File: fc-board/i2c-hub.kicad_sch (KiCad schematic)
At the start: 54 parts, among them U2 PCT2075TP_147, U3 MAX11617EEE+, U4 DS3231M+TRL, U5 TLV9004QPWRQ1, U6 ADS122C04IPWR

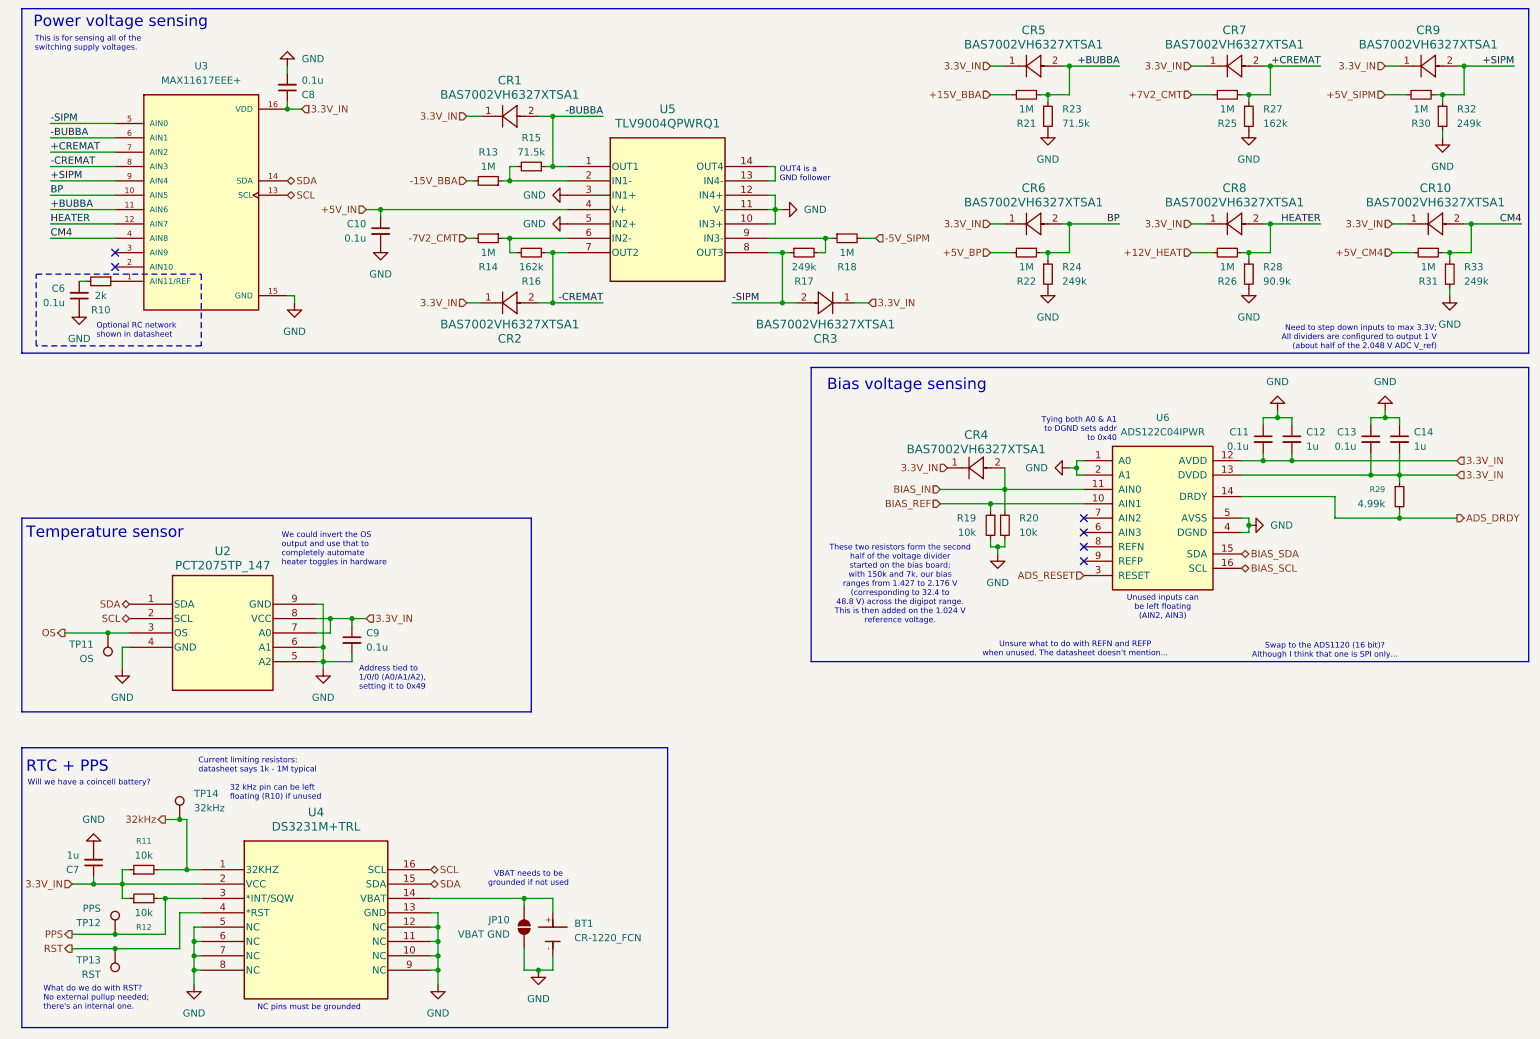
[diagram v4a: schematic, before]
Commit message: Fixed PCIe routing, voltage sensing, added DAQ toggle, LCT interrupt, bias sensing resistors, SD card, and more
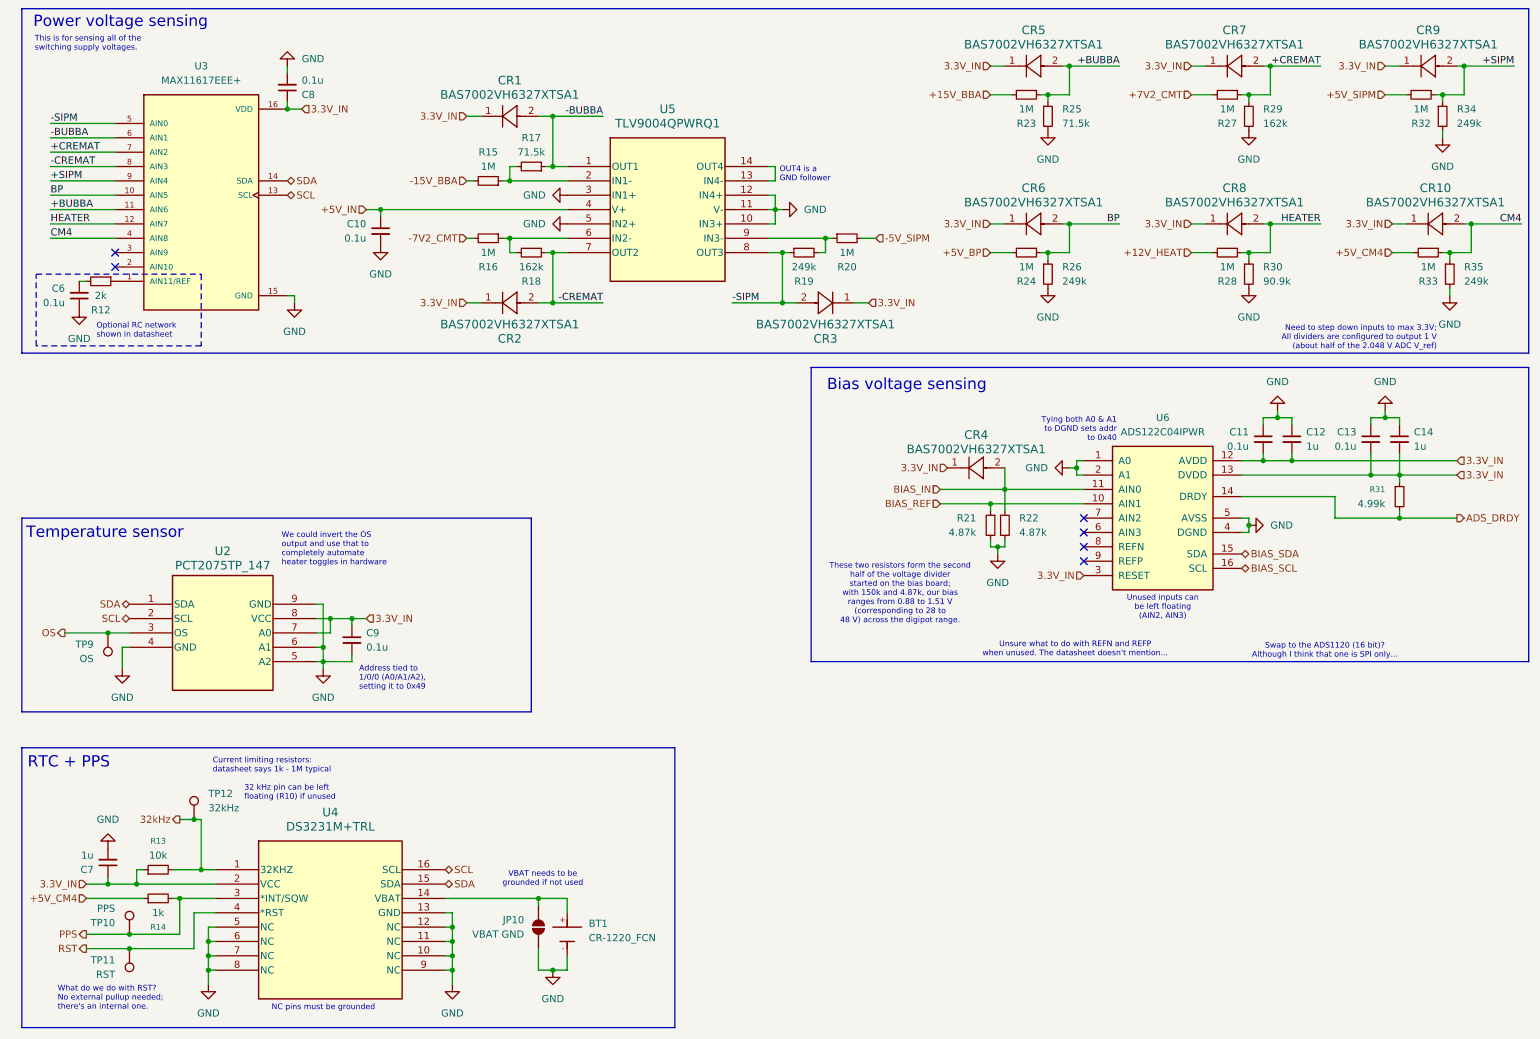
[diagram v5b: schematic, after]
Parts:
- R14: renamed from R12; value 10k -> 1k
- R21: renamed from R19; value 10k -> 4.87k
- R22: renamed from R20; value 10k -> 4.87k
- renumbered R10 to R12, R11 to R13, R13 to R15, R14 to R16, R15 to R17, R16 to R18, R17 to R19, R18 to R20, R21 to R23, R22 to R24, R23 to R25, R24 to R26, R25 to R27, R26 to R28, R27 to R29, R28 to R30, R29 to R31, R30 to R32, R31 to R33, R32 to R34, R33 to R35, TP12 to TP10, TP13 to TP11, TP14 to TP12, TP11 to TP9
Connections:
- net ADS_RESET is gone; now on net 3.3V_IN: U6.3 (RESET)
- net +5V_CM4: now also R14.1
- net 3.3V_IN: no longer R14.1
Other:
- note added: "These two resistors form the second half of the voltage divider started on the bias board; with 150k and 4.87k, our bias ranges from 0.88 to 1.51 V (corresponding to 28 to 48 V) across the digipot range."
- note removed: "These two resistors form the second half of the voltage divider started on the bias board; with 150k and 7k, our bias ranges from 1.427 to 2.176 V (corresponding to 32.4 to 48.8 V) across the digipot range. This is then added on the 1.024 V reference voltage."
- note removed: "Will we have a coincell battery?"
- moved on the sheet: BT1, C7, JP10, R13, R14, TP10, TP11, TP12, U4

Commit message: Fleshed out part numbers and design rules
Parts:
- BT1: now left out of the parts list
- TP10, TP11, TP12, TP9: symbol Connector:TestPoint -> fc-board:TestPoint; now left out of the parts list
